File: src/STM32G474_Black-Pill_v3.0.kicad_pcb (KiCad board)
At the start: 2 copper layers, 63.5 x 25.4 mm, 46 parts, among them J101 USB_C_Receptacle_USB2.0, J102 Conn_01x20, J103 Conn_01x20, J104 Conn_01x04, SW101 SW_Push, SW102 SW_Push, SW103 SW_Push, U101 W25Q32JVSS, U102 STM32G474RETx, U103 AP7343xx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

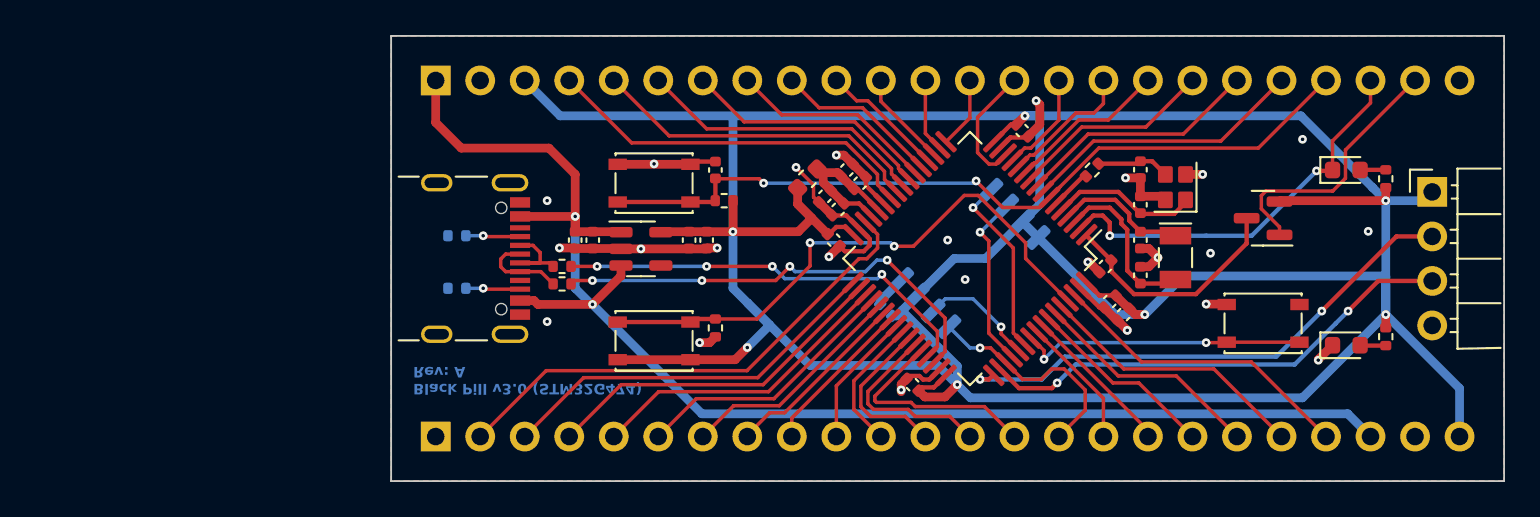
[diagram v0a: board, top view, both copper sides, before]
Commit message: Mod: STM32G474_Black-Pill_v3.0.kicad_pcb, changed footprint of STM32G474 and the whole PCB has to be adjusted.
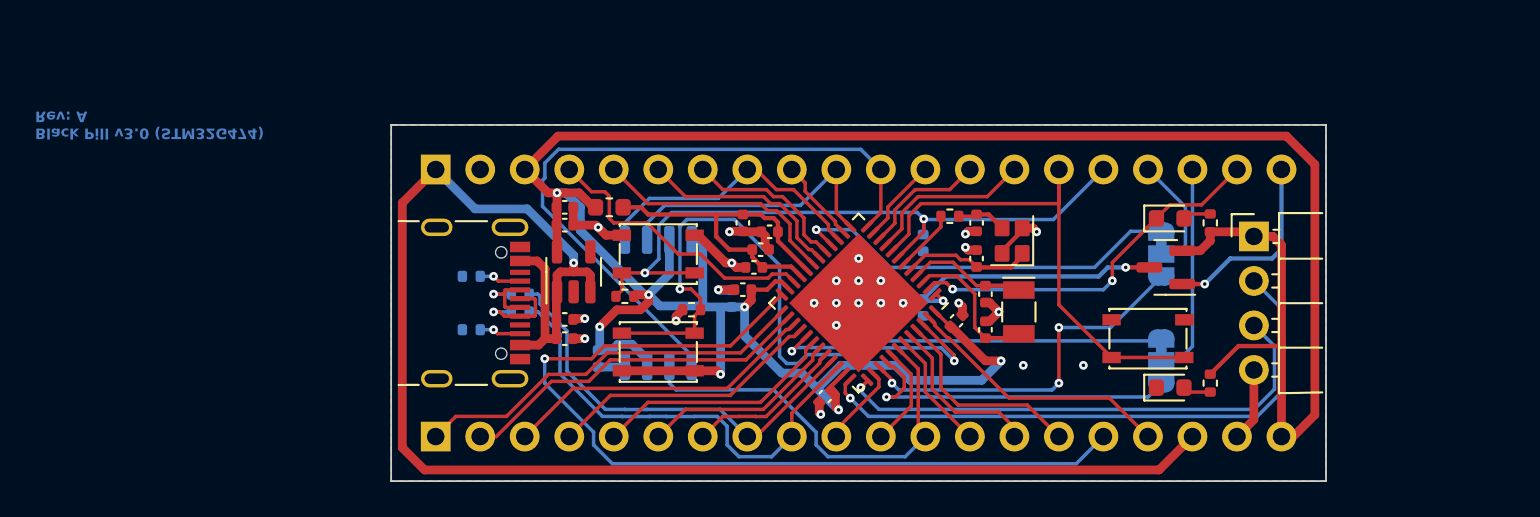
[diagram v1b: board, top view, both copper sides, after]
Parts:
- removed C111: 100nF, Capacitor_SMD:C_0402_1005Metric
- added JP101: SolderJumper_3_Bridged12, Jumper:SolderJumper-3_P1.3mm_Bridged12_RoundedPad1.0x1.5mm_NumberLabels, B.Cu at (143.0, 98.8)
- added JP102: SolderJumper_3_Bridged12, Jumper:SolderJumper-3_P1.3mm_Bridged12_RoundedPad1.0x1.5mm_NumberLabels, B.Cu at (143.0, 104.9)
- C104, C107, C112, R104, R105: moved to B.Cu
- J102, J103: footprint Connector_PinHeader_2.54mm:PinHeader_1x24_P2.54mm_Vertical -> Connector_PinHeader_2.54mm:PinHeader_1x20_P2.54mm_Vertical
- U102: value STM32G474RETx -> STM32G474CEUx; footprint Package_QFP:LQFP-64_10x10mm_P0.5mm -> Package_DFN_QFN:QFN-48-1EP_7x7mm_P0.5mm_EP5.6x5.6mm
- moved C107 22.4 mm to (118.5, 101.3), turned to 90 degrees
- moved C110 18.3 mm to (119.1, 100.8), turned to 180 degrees
- moved U101 18.0 mm to (114.3, 101.6), turned to 90 degrees
- moved C101 16.7 mm to (110.9, 104.8), turned to -90 degrees
- moved G*** 14.7 mm to (101.1, 101.6)
- moved C104 12.6 mm to (129.4, 98.2), turned to -90 degrees
- moved L101 11.4 mm to (111.5, 96.1), turned to 0 degrees
- moved C112 10.7 mm to (129.4, 101.9), turned to -90 degrees
- moved J104 10.5 mm to (148.3, 97.8)
- moved D103 10.4 mm to (143.5, 96.8)
- moved R107 10.4 mm to (145.8, 106.2)
- moved D101 10.3 mm to (143.5, 106.4)
- moved R109 10.3 mm to (145.8, 97.0)
- moved C102 9.84 mm to (132.5, 99.1)
- moved C103 9.83 mm to (132.5, 97.0)
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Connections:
- J102 pad 1: GND -> /PB12
- J102 pad 10: /PC8 -> /PA15
- J102 pad 11: /PC9 -> /PB3
- J102 pad 12: /PA8 -> /PB4
- J102 pad 13: /PA9 -> /PB5
- J102 pad 14: /PA10 -> /PB6
- J102 pad 15: /PA15 -> /PB7
- J102 pad 16: /PB3 -> /PB11
- J102 pad 17: /PB4 -> /PB9
- J102 pad 18: /PB5 -> +5V
- J102 pad 19: /PB6 -> GND
- J102 pad 2: /PB10 -> /PB13
- J102 pad 20: /PB7 -> +3.3V
- J102 pad 3: /PB11 -> /PB14
- J102 pad 4: /PB12 -> /PB15
- J102 pad 5: /PB13 -> /PA8
- J102 pad 6: /PB14 -> /PA9
- J102 pad 7: /PB15 -> /PA10
- J102 pad 8: /PC6 -> /PA11
- J102 pad 9: /PC7 -> /PA12
- J103 pad 10: /PA6 -> /PA5
- J103 pad 11: /PA5 -> /PA4
- J103 pad 12: /PA4 -> /PA3
- J103 pad 13: /PA3 -> /PA2
- J103 pad 14: /PA2 -> /PA1
- J103 pad 15: /PA1 -> /PA0
- J103 pad 16: /PA0 -> NRST
- J103 pad 17: /PC3 -> /Pin17
- J103 pad 18: /PC2 -> /Pin18
- J103 pad 19: /PC1 -> /PC13
- J103 pad 20: /PC0 -> VB
- J103 pad 4: /PB2 -> /PB10
- J103 pad 5: /PB1 -> /PB2
- J103 pad 6: /PB0 -> /PB1
- J103 pad 7: /PC5 -> /PB0
- J103 pad 8: /PC4 -> /PA7
- J103 pad 9: /PA7 -> /PA6
- R108 pad 1: /BOOT -> /PB8
- SW102 pad 1: /BOOT -> /PB8
- SW103 pad 2: /PD2 -> /PA0
- U101 pad 1: /PA15 -> /PA4
- U101 pad 2: /SPI_{3}.MISO -> /PB4
- U101 pad 5: /SPI_{3}.MOSI -> /PA7
- U101 pad 6: /SPI_{3}.SCK -> /PA5
- U102 pad 10: /PC2 -> /PA2
- U102 pad 11: /PC3 -> /PA3
- U102 pad 12: /PA0 -> /PA4
- U102 pad 13: /PA1 -> /PA5
- U102 pad 14: /PA2 -> /PA6
- U102 pad 15: GND -> /PA7
- U102 pad 16: +3.3V -> /PC4
- U102 pad 17: /PA3 -> /PB0
- U102 pad 18: /PA4 -> /PB1
- U102 pad 19: /PA5 -> /PB2
- U102 pad 20: /PA6 -> VREF
- U102 pad 21: /PA7 -> VREF
- U102 pad 22: /PC4 -> /PB10
- U102 pad 23: /PC5 -> +3.3V
- U102 pad 24: /PB0 -> /PB11
- U102 pad 25: /PB1 -> /PB12
- U102 pad 26: /PB2 -> /PB13
- U102 pad 27: GND -> /PB14
- U102 pad 28: VREF -> /PB15
- U102 pad 29: VREF -> /PC6
- U102 pad 30: /PB10 -> /PA8
- U102 pad 31: GND -> /PA9
- U102 pad 32: +3.3V -> /PA10
- U102 pad 33: /PB11 -> /PA11
- U102 pad 34: /PB12 -> /PA12
- U102 pad 35: /PB13 -> +3.3V
- U102 pad 36: /PB14 -> /SWDIO
- U102 pad 37: /PB15 -> /SWCLK
- U102 pad 38: /PC6 -> /PA15
- U102 pad 39: /PC7 -> /PC10
- U102 pad 40: /PC8 -> /PC11
- U102 pad 41: /PC9 -> /PB3
- U102 pad 42: /PA8 -> /PB4
- U102 pad 43: /PA9 -> /PB5
- U102 pad 44: /PA10 -> /PB6
- U102 pad 45: /PA11 -> /PB7
- U102 pad 46: /PA12 -> /PB8
- U102 pad 47: GND -> /PB9
- U102 pad 49: /SWDIO -> GND
- U102 pad 8: /PC0 -> /PA0
- U102 pad 9: /PC1 -> /PA1
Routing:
- net +3.3V: track 218.4 -> 168.7 mm
- net /PB8: track 0.00 -> 37.1 mm, vias 0 -> 2
- net /PA4: track 4.19 -> 38.7 mm
- net /BOOT: track 32.6 -> 0.00 mm, vias 2 -> 0
- net /PB11: track 22.4 -> 51.3 mm, vias 0 -> 1
- net GND: track 52.5 -> 28.2 mm, vias 24 -> 25
- net /PA0: track 7.65 -> 29.3 mm
- net /PC10: track 0.00 -> 21.3 mm, vias 0 -> 3
- net /PC11: track 0.00 -> 19.3 mm, vias 0 -> 1
- net /PD2: track 16.5 -> 0.00 mm, vias 2 -> 0
- net /PC0: track 16.2 -> 0.00 mm
- net /PB4: track 8.80 -> 23.9 mm
- net /PC5: track 14.2 -> 0.00 mm
- net /PC1: track 13.9 -> 0.00 mm
- net /Pin18: track 0.00 -> 12.2 mm
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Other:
- board size 63.5 x 25.4 mm -> 53.3 x 20.3 mm

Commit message: Mod: PCB and Schematic, re-exported all files.
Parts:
- added JP103: SolderJumper_2_Bridged, Jumper:SolderJumper-2_P1.3mm_Bridged_RoundedPad1.0x1.5mm, B.Cu at (140.3, 101.9)
- C104, C107, C112: moved to F.Cu
- moved C107 15.2 mm to (133.0, 105.9), turned to -90 degrees
- moved C112 11.4 mm to (140.7, 100.1)
- moved C117 1.61 mm to (118.6, 99.1), turned to 90 degrees
- moved C120 1.02 mm to (119.8, 97.0), turned to -90 degrees
- moved C118 0.51 mm to (118.6, 97.0), turned to -90 degrees
- moved C119 0.51 mm to (119.8, 99.1), turned to 90 degrees
- moved JP101 0.51 mm to (143.0, 98.3)
- moved C104 0.40 mm to (129.3, 97.8), turned to 0 degrees
- moved R103 0.40 mm to (112.8, 101.3)
- moved R108 0.40 mm to (115.8, 101.9)
- moved C102 0.38 mm to (132.8, 99.1)
- moved C103 0.38 mm to (132.8, 97.0)
- moved R106 0.38 mm to (131.3, 96.6)
- moved Y101 0.38 mm to (134.9, 98.0)
- moved G*** 0.25 mm to (101.1, 101.9)
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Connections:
- C107 pad 1: +3.3V -> /+3.3V_{MCU}
- C108 pad 1: +3.3V -> /+3.3V_{MCU}
- C109 pad 1: +3.3V -> /+3.3V_{MCU}
- C110 pad 1: +3.3V -> /+3.3V_{MCU}
- U102 pad 23: +3.3V -> /+3.3V_{MCU}
- U102 pad 35: +3.3V -> /+3.3V_{MCU}
- U102 pad 48: +3.3V -> /+3.3V_{MCU}
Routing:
- net +3.3V: track 168.7 -> 18.0 mm
- net /+3.3V_{MCU}: track 0.00 -> 37.9 mm, vias 0 -> 4
- net /PB11: track 51.3 -> 33.1 mm
- net /PB8: track 37.1 -> 27.4 mm
- net /PA4: track 38.7 -> 33.6 mm
- net GND: track 28.2 -> 30.9 mm, vias 25 -> 34
- net VBAT: track 15.6 -> 14.1 mm
- net /PC10: track 21.3 -> 22.7 mm
- net /PC13: track 21.3 -> 22.6 mm
- net VREF: track 19.9 -> 18.7 mm
- net /PB9: track 15.4 -> 16.4 mm
- net /PA7: track 16.2 -> 17.1 mm
- net /PC14: track 8.45 -> 7.76 mm
- net /PA11: track 24.0 -> 24.7 mm
- net /PA12: track 25.9 -> 26.6 mm
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- added copper zone on B.Cu, net +3.3V
- added copper zone on F.Cu, net +3.3V
- added copper zone on In2.Cu, net +3.3V
- added copper zone on In1.Cu, net GND
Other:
- copper layers 2 -> 4
- board text added: "3V3"
- board text added: "5V"
- board text added: "A0"
- board text added: "A1"
- board text added: "A10"
- board text added: "A11"
- board text added: "A12"
- board text added: "A15"
- board text added: "A2"
- board text added: "A3"
- board text added: "A4"
- board text added: "A5"
- board text added: "A6"
- board text added: "A7"
- board text added: "A8"
- board text added: "A9"
- board text added: "B0"
- board text added: "B1"
- board text added: "B10"
- board text added: "B11"
- board text added: "B12"
- board text added: "B13"
- board text added: "B14"
- board text added: "B15"
- board text added: "B2"
- board text added: "B3"
- board text added: "B4"
- board text added: "B5"
- board text added: "B6"
- board text added: "B7"
- board text added: "B9"
- board text added: "BOOT0"
- board text added: "BTN"
- board text added: "C10"
- board text added: "C11"
- board text added: "C13"
- board text added: "C4"
- board text added: "C6"
- board text added: "GND"
- board text added: "LED"
- board text added: "MCU PWR"
- board text added: "NRST"
- board text added: "P17"
- board text added: "P18"
- board text added: "PWR"
- board text added: "RST"
- board text added: "VB"
